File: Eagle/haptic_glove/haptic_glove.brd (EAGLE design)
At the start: 100 x 80 mm, 58 parts, among them U1 DRV2605L, U2 DRV2605L, U3 DRV2605L, U4 DRV2605L, U5 MPU-6050-1, U6 MCP73833, X1 TSW-121-07-G-S, X2 TSW-121-07-G-S, X3 TSW-121-07-G-S, X4 TSW-121-07-G-S

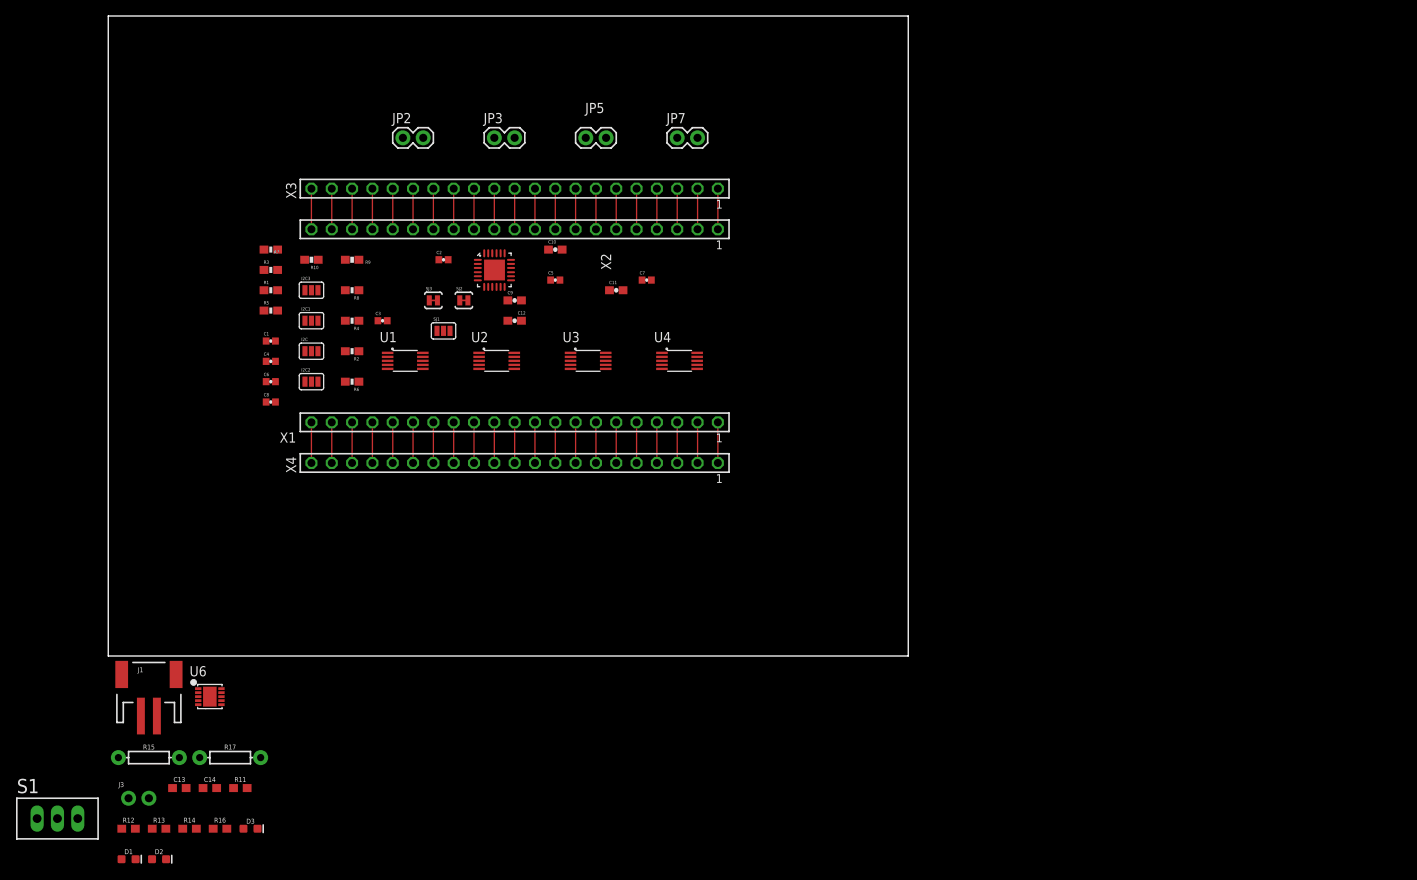
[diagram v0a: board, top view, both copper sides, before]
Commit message: board schematic update
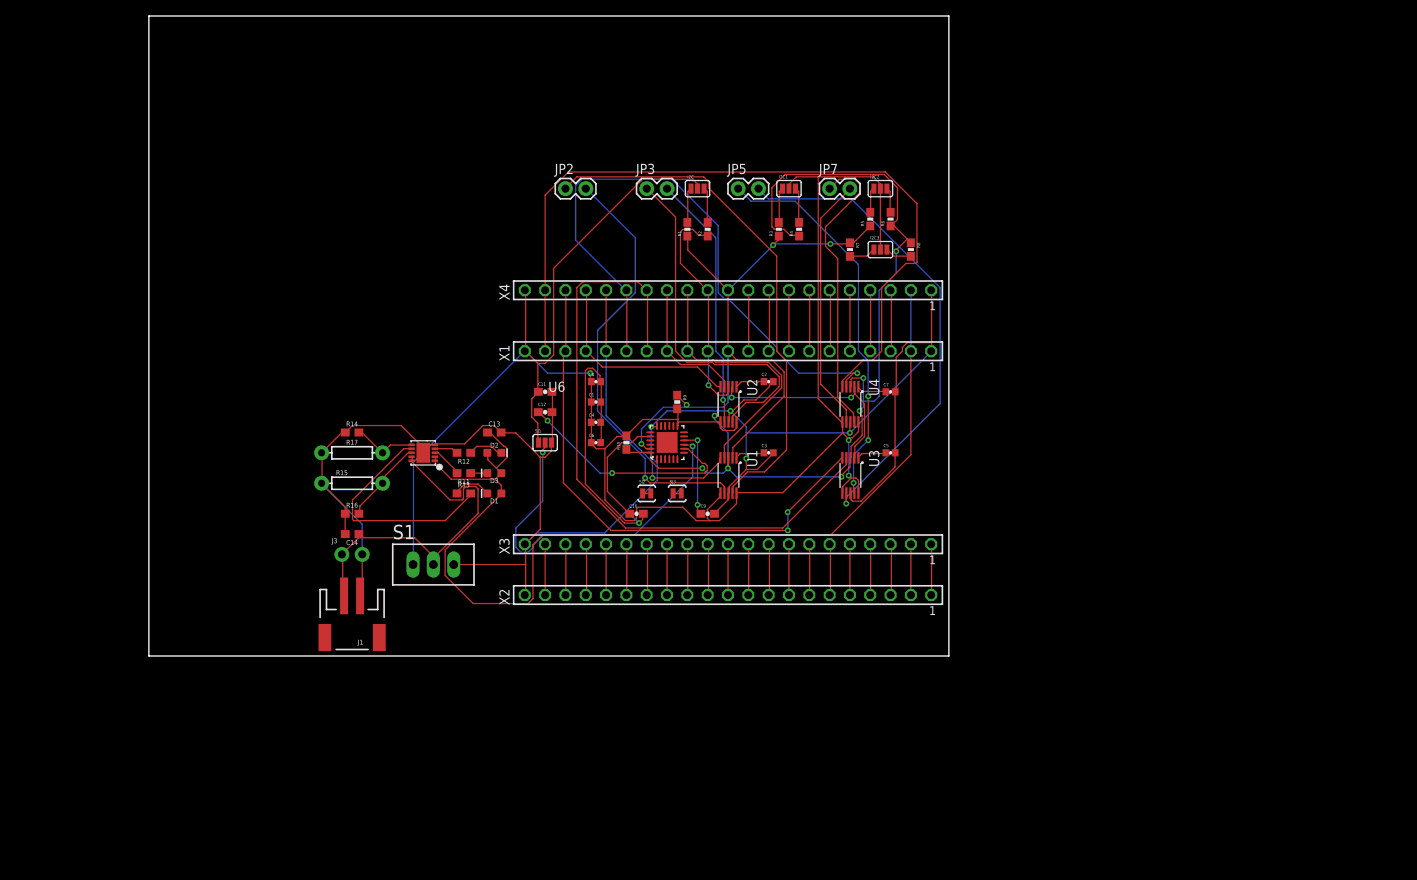
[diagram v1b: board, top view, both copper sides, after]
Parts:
- moved R5 75.8 mm to (90.2, 54.6), turned to 90 degrees
- moved I2C2 75.1 mm to (91.4, 58.4)
- moved R7 72.4 mm to (87.6, 50.8), turned to 270 degrees
- moved I2C3 71.3 mm to (91.4, 50.8)
- moved R6 70.3 mm to (92.7, 54.6), turned to 90 degrees
- moved R8 70.0 mm to (95.2, 50.8), turned to 270 degrees
- moved D2 65.9 mm to (43.2, 25.4)
- moved D1 64.7 mm to (43.2, 20.3), turned to 180 degrees
- moved R3 63.7 mm to (78.7, 53.3), turned to 90 degrees
- moved R12 63.0 mm to (39.4, 25.4), turned to 180 degrees
- moved I2C1 61.9 mm to (80.0, 58.4)
- moved C13 59.4 mm to (43.2, 27.9)
- moved R4 57.0 mm to (81.3, 53.3), turned to 90 degrees
- moved S1 56.7 mm to (35.6, 11.4)
- moved R13 56.6 mm to (39.4, 20.3)
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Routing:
- net GND: track 10.2 -> 266.2 mm, vias 0 -> 5
- net VCC: track 5.08 -> 249.3 mm, vias 0 -> 3
- net SDA: track 5.08 -> 144.3 mm, vias 0 -> 8
- net N$60: track 5.08 -> 127.0 mm
- net SCL: track 5.08 -> 111.8 mm, vias 0 -> 6
- net N$30: track 5.08 -> 97.0 mm
- net N$20: track 5.08 -> 81.6 mm
- net N$29: track 5.08 -> 76.8 mm, vias 0 -> 1
- net N$6: track 0.00 -> 65.8 mm
- net N$21: track 5.08 -> 66.8 mm, vias 0 -> 2
- net N$23: track 0.00 -> 61.0 mm, vias 0 -> 1
- net N$7: track 0.00 -> 54.3 mm, vias 0 -> 1
- net N$22: track 0.00 -> 48.8 mm, vias 0 -> 3
- net ADO: track 0.00 -> 46.1 mm, vias 0 -> 2
- net N$13: track 0.00 -> 45.5 mm
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
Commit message: Updated schematic and board design
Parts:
- moved J1 85.9 mm to (96.5, 52.1), turned to 270 degrees
- moved S1 77.3 mm to (92.7, 63.5)
- moved J3 74.1 mm to (87.6, 50.8), turned to 90 degrees
- moved C14 72.6 mm to (83.8, 58.4)
- moved R15 71.9 mm to (94.0, 43.2)
- moved R16 71.9 mm to (94.0, 39.4)
- moved R17 61.3 mm to (85.1, 39.4)
- moved R14 60.2 mm to (85.1, 35.6)
- moved U6 56.4 mm to (86.4, 47.0), turned to 0 degrees
- moved JP2 56.1 mm to (96.5, 24.1), flipped to the bottom
- moved R13 48.3 mm to (82.5, 41.9)
- moved R11 46.0 mm to (80.0, 44.5), turned to 0 degrees
- moved R12 45.5 mm to (81.3, 43.2), turned to 0 degrees
- moved JP3 44.2 mm to (90.2, 24.1), flipped to the bottom
- moved C9 43.2 mm to (30.5, 35.6), turned to 180 degrees
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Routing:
- net GND: track 266.2 -> 97.9 mm, vias 5 -> 0
- net N$60: track 127.0 -> 25.3 mm
- net N$11: track 17.1 -> 90.1 mm, vias 0 -> 1
- net N$21: track 66.8 -> 108.6 mm, vias 2 -> 1
- net SDA: track 144.3 -> 103.5 mm, vias 8 -> 0
- net ADO: track 46.1 -> 7.99 mm, vias 2 -> 0
- net N$23: track 61.0 -> 24.5 mm, vias 1 -> 2
- net N$30: track 97.0 -> 65.7 mm, vias 0 -> 1
- net N$20: track 81.6 -> 52.2 mm, vias 0 -> 1
- net N$22: track 48.8 -> 21.8 mm, vias 3 -> 1
- net N$12: track 26.4 -> 53.2 mm, vias 0 -> 1
- net VIO: track 28.8 -> 4.86 mm, vias 2 -> 0
- net N$6: track 65.8 -> 42.9 mm, vias 0 -> 2
- net VCC: track 249.3 -> 270.5 mm, vias 3 -> 7
- net N$5: track 35.7 -> 56.8 mm, vias 1 -> 3
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- added copper zone on layer 16, net GND
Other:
- board size 100 x 80 mm -> 81 x 57.1 mm
